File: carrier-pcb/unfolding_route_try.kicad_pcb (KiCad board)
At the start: 2 copper layers, 57 x 74.6 mm, 71 parts, among them J1 USB4125-GF-A_REVA, J2 Conn_01x01_Female, J3 1-338068-8, J4 Conn_01x01_Female, J5 Conn_01x01_Female, J6 Conn_01x01_Female, U1 TCA9548APWR, U10 DRV2605LDGS, U11 DRV2605LDGS, U12 BMX160, U13 USBLC6-2SC6, U2 TCA9548APWR, U3 DRV2605LDGS, U4 DRV2605LDGS, U5 DRV2605LDGS, U6 DRV2605LDGS, U7 DRV2605LDGS, U8 DRV2605LDGS, U9 DRV2605LDGS

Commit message: Bestellte Version
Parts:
- moved C22 1.30 mm to (136.2, 90.2)
- moved J4 0.20 mm to (138.0, 94.1)
- moved J5 0.20 mm to (139.4, 94.1)
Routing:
- net +5V: track 73.7 -> 78.8 mm, vias 0 -> 2
- net GND: track 70.4 -> 72.8 mm

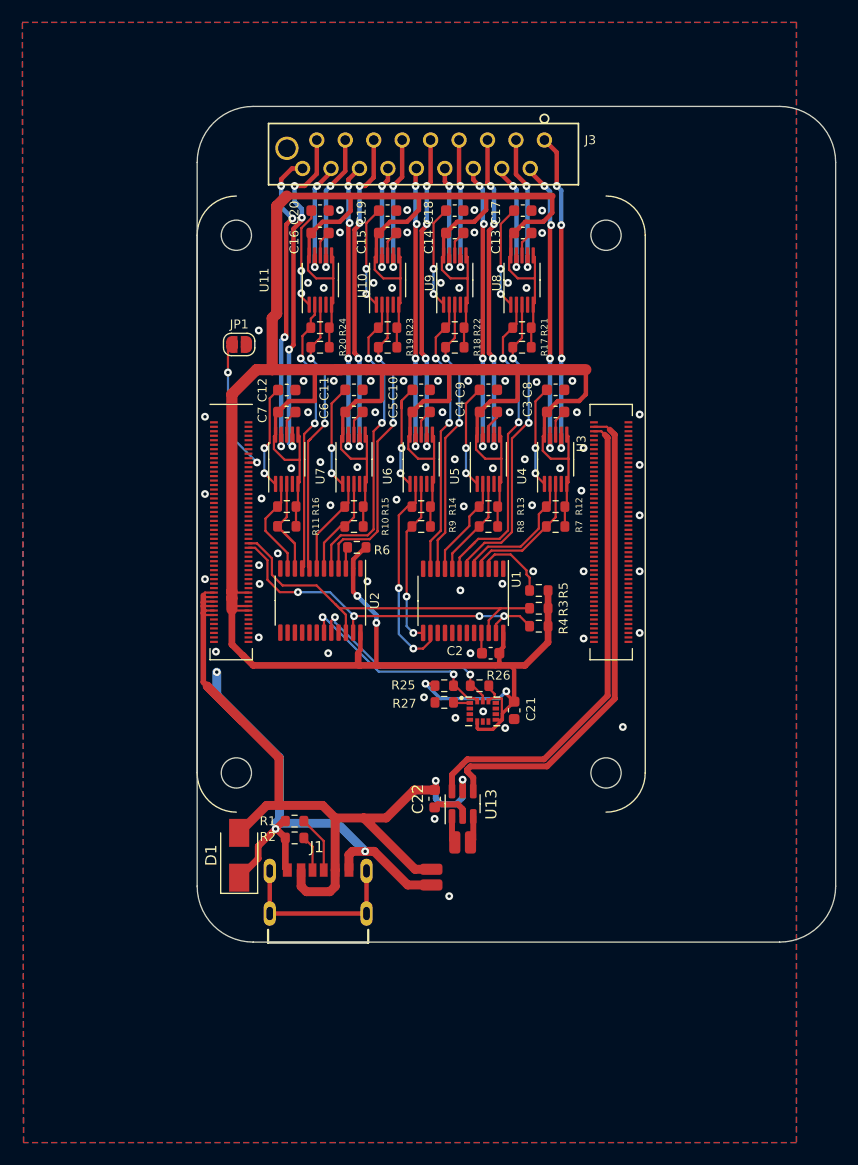
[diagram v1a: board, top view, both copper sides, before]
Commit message: Added compass, added LEDs, changed USB TVS diode, fixed power TVS diode direction, moved accelerometer, misc minor improvements
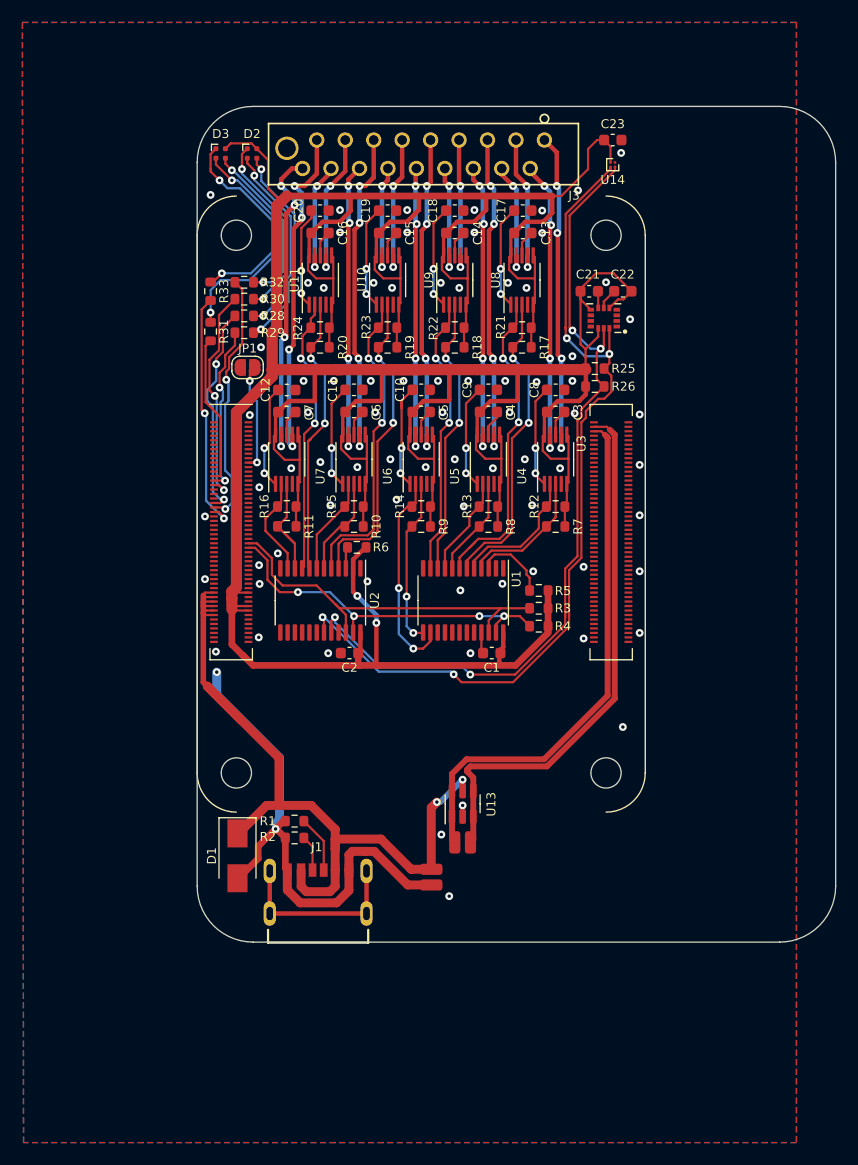
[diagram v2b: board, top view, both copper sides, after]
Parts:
- removed R27: 2K2, Resistor_SMD:R_0603_1608Metric
- added C1: 1u, Capacitor_SMD:C_0603_1608Metric, F.Cu at (141.3, 77.2)
- added C23: 2.2u, Capacitor_SMD:C_0603_1608Metric, F.Cu at (152.1, 31.4)
- added D2: UHD1110-FKA, LED_SMD:LED_Lumex_SML-LX0404SIUPGUSB, F.Cu at (119.9, 32.6)
- added D3: UHD1110-FKA, LED_SMD:LED_Lumex_SML-LX0404SIUPGUSB, F.Cu at (117.1, 32.6)
- added R28: 1K, Resistor_SMD:R_0603_1608Metric, F.Cu at (119.2, 47.1)
- added R29: 220, Resistor_SMD:R_0603_1608Metric, F.Cu at (119.2, 48.6)
- added R30: 150, Resistor_SMD:R_0603_1608Metric, F.Cu at (119.2, 45.6)
- added R31: 1K, Resistor_SMD:R_0603_1608Metric, F.Cu at (116.2, 48.5)
- added R32: 220, Resistor_SMD:R_0603_1608Metric, F.Cu at (119.2, 44.1)
- added R33: 150, Resistor_SMD:R_0603_1608Metric, F.Cu at (116.2, 44.9)
- added U14: MMC5633NJL, Package_BGA:WLP-4_0.86x0.86mm_P0.4mm, F.Cu at (152.1, 33.6)
- D1: value SMA6J5.0A -> SMBJ5A
- U12: value BMX160 -> LSM6DSxx
- moved C22 48.3 mm to (153.0, 44.9), turned to 180 degrees
- moved C21 38.0 mm to (150.0, 44.9), turned to 0 degrees
- moved U12 36.7 mm to (151.3, 47.3), turned to 180 degrees
- moved R25 31.3 mm to (150.5, 51.8)
- moved R26 28.6 mm to (150.5, 53.4), turned to 0 degrees
- moved C2 12.6 mm to (128.6, 77.2)
- moved JP1 2.18 mm to (119.5, 51.7), turned to 180 degrees
- moved D1 0.16 mm to (118.6, 95.3), turned to -90 degrees
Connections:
- net SCL_bmx160 renamed SCL_IMU
- net SDA_bmx160 renamed SDA_IMU
- C22 pad 1: +5V -> +3V3
- D1 pad 1: GND -> +5V
- D1 pad 2: +5V -> GND
- Module1 pad 103: USB_D-out -> USB_D-
- Module1 pad 105: USB_D+out -> USB_D+
- Module1 pad 25: unconnected-(Module1-Pad25) -> LED2R
- Module1 pad 27: unconnected-(Module1-Pad27) -> LED1G
- Module1 pad 29: unconnected-(Module1-Pad29) -> LED1B
- Module1 pad 37: unconnected-(Module1-Pad37) -> LED1R
- Module1 pad 39: unconnected-(Module1-Pad39) -> LED2G
- Module1 pad 41: unconnected-(Module1-Pad41) -> LED2B
- U12 pad 1: Net-(R27-Pad1) -> GND
- U13 pad 4: USB_D-out -> USB_D-
- U13 pad 6: USB_D+out -> USB_D+
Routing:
- net SDA_IMU: track 19.0 -> 78.8 mm, vias 2 -> 4
- net SCL_IMU: track 19.2 -> 75.4 mm, vias 2 -> 4
- net USB_D-: track 2.70 -> 48.6 mm
- net USB_D+: track 2.98 -> 48.1 mm
- net USB_D-out: track 43.0 -> 0.00 mm
- net USB_D+out: track 42.8 -> 0.00 mm
- net LED2G: track 0.00 -> 22.9 mm, vias 0 -> 2
- net LED2B: track 0.00 -> 21.8 mm, vias 0 -> 2
- net Net-(R31-Pad2): track 0.00 -> 21.3 mm, vias 0 -> 2
- net LED1B: track 0.00 -> 19.6 mm, vias 0 -> 2
- net LED1R: track 0.00 -> 19.2 mm, vias 0 -> 2
- net Net-(R33-Pad2): track 0.00 -> 19.1 mm, vias 0 -> 2
- net Net-(R29-Pad2): track 0.00 -> 18.7 mm, vias 0 -> 2
- net Net-(R28-Pad2): track 0.00 -> 17.6 mm, vias 0 -> 2
- net Net-(R30-Pad2): track 0.00 -> 17.0 mm, vias 0 -> 2
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
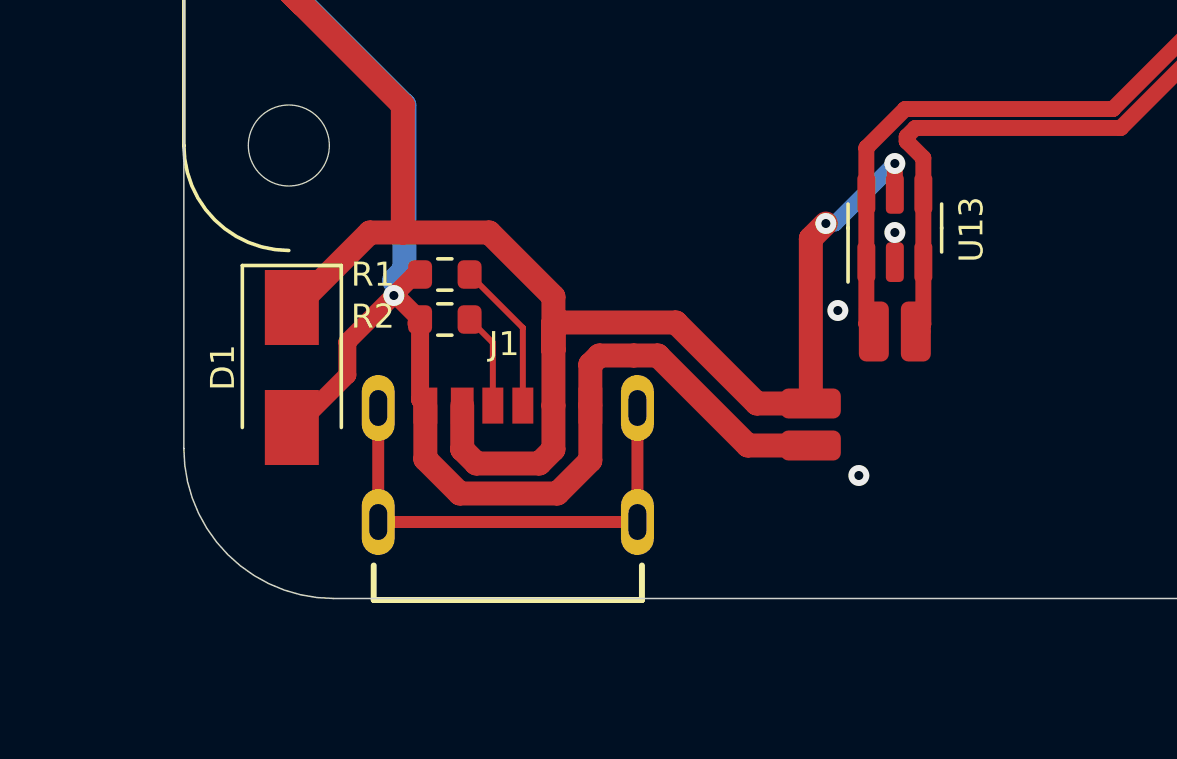
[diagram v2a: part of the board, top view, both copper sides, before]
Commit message: Added Pico-SPOX connector for 5V fan
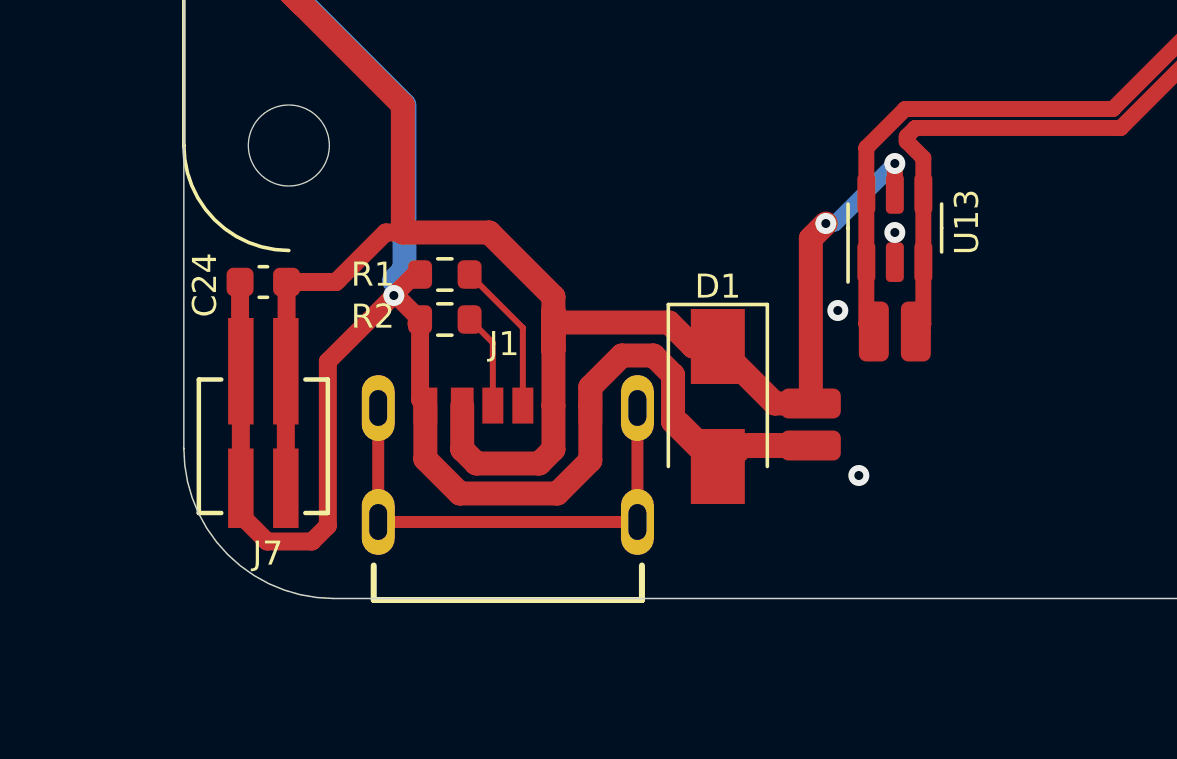
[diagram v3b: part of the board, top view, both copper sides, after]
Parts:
- added C24: 1u, Capacitor_SMD:C_0603_1608Metric, F.Cu at (117.7, 92.5)
- added J7: Fan, Pico-Spox:PICOspox-2-v, F.Cu at (117.7, 97.2)
- D1: value SMBJ5A -> SMBJ5.0A
- U13: value USBLC6-2SC6 -> WE 82400102
- moved D1 14.3 mm to (132.8, 96.6)
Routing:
- net GND: track 73.8 -> 93.0 mm
- net +5V: track 73.4 -> 81.1 mm

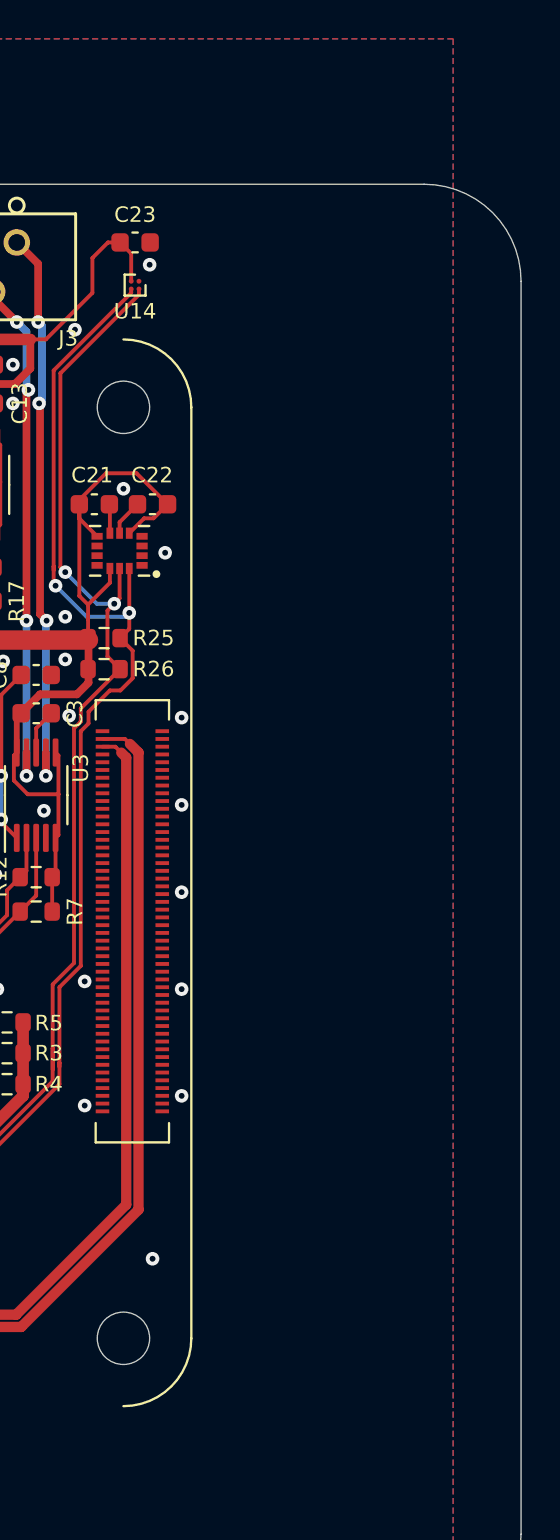
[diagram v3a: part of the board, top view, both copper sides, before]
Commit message: Add milling for camera fixation rubber band. Add silkscreen text "UnfoldingSpace Carrier Board Rev. 2"
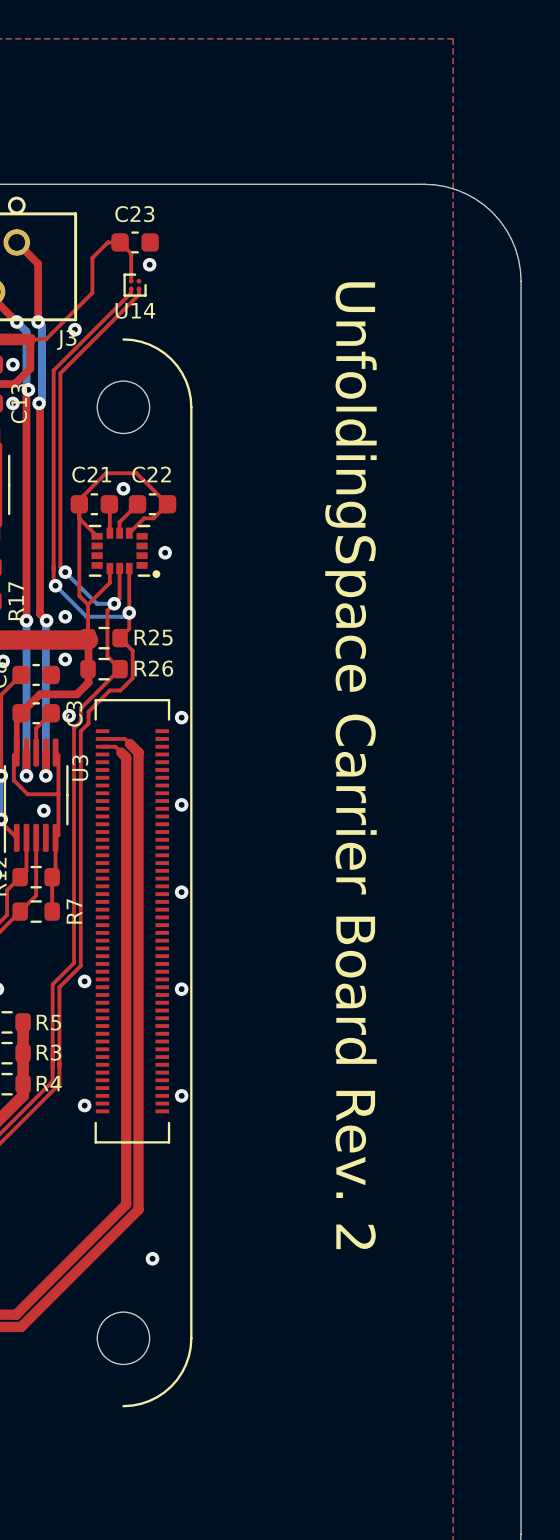
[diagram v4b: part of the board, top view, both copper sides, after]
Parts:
- added ?: , , F.Cu at (155.4, 37.8)
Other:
- board text added: "UnfoldingSpace Carrier Board Rev. 2"
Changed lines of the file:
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@@
     )
+  )
+  (footprint "" (layer "F.Cu")
+    (at 155.4 37.8 90)
+    (fp_text reference "" (at 0 0 90) (layer "F.SilkS")
+      (effects (font (size 1.27 1.27) (thickness 0.15)))
+    )
+    (fp_text value "" (at 0 0 90) (layer "F.SilkS")
+      (effects (font (size 1.27 1.27) (thickness 0.15)))
+    )
+    (pad "" np_thru_hole oval locked (at 0 0 90) (size 3.4 1.2) (drill oval 3.4 1.2) (layers F&B.Cu *.Mask)
+      (solder_mask_margin 0.1) (clearance 0.1))
   )
   (footprint "Resistor_SMD:R_0603_1608Metric" (layer "F.Cu")
@@
   (gr_line (start 172 98) (end 172 33.4) (layer "Edge.Cuts") (width 0.05))
   (gr_arc (start 120 98) (end 115 98) (angle -90) (layer "Edge.Cuts") (width 0.05))
+  (gr_text "UnfoldingSpace Carrier Board Rev. 2" (at 163.4 58.4 270) (layer "F.SilkS")
+    (effects (font (size 2 2) (thickness 0.34)))
+  )
   (segment (start 124.898022 43.029151) (end 124.898022 41.801978) (width 0.2) (layer "F.Cu") (net 68))
   (segment (start 130 62.1) (end 130.15 61.95) (width 0.2) (layer "F.Cu") (net 68))
